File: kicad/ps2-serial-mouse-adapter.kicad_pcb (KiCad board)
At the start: 2 copper layers, 68.9 x 34 mm, 8 parts, among them U1 Arduino_Nano, U2 MAX3232_HW027

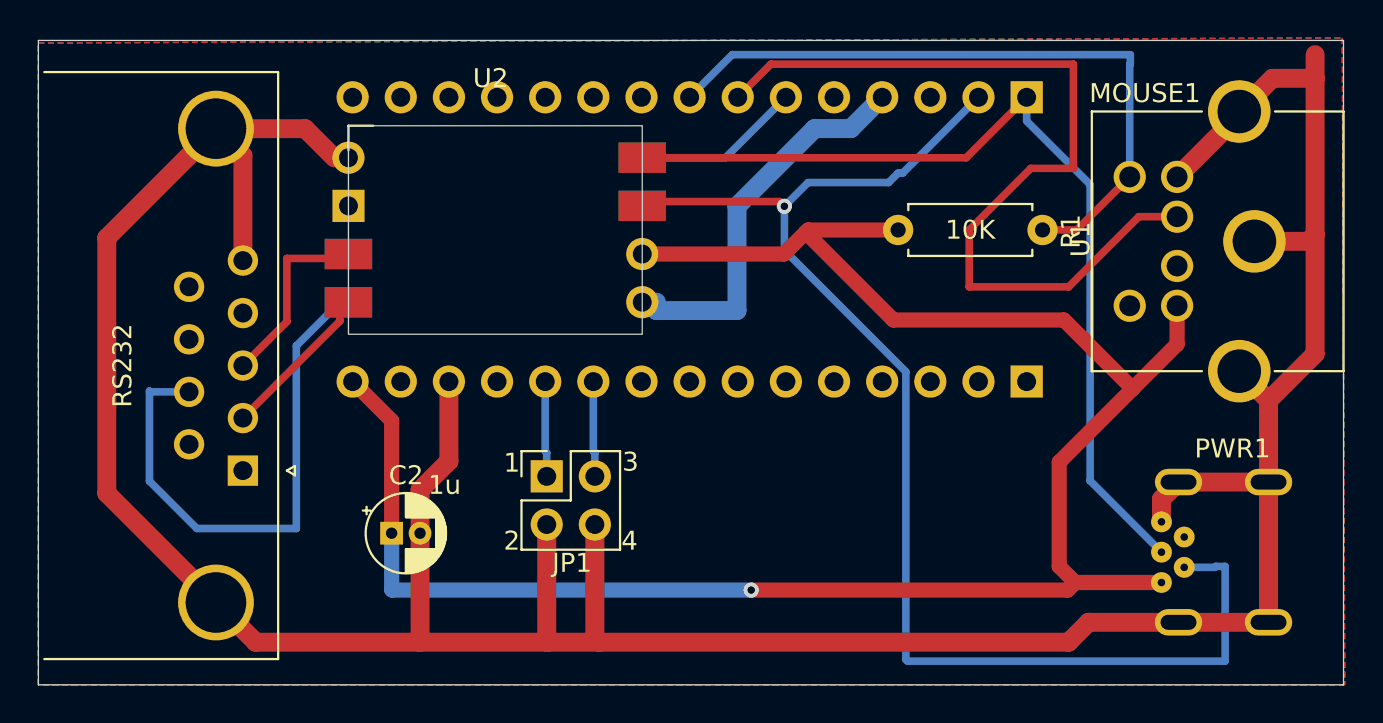
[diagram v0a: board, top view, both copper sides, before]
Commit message: flip arduino and fix pinout. Change usb-mini plug to a pinheader row. Add pads for U2
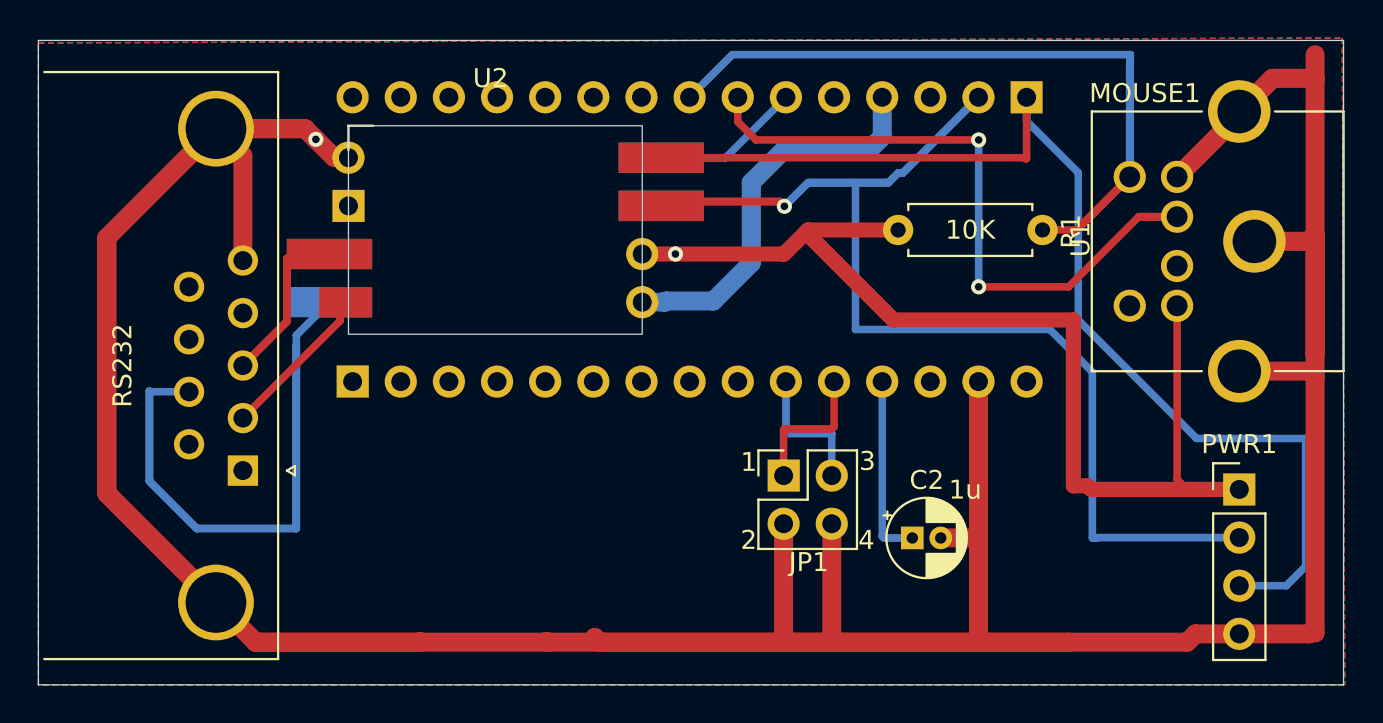
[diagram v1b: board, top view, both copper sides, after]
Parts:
- PWR1: footprint ps2-serial-mouse-adapter:USB_Mini-B-Jing_Extension_LSCS_C46398 -> PinHeader_1x04_P2.54mm_Vertical
- moved C2 27.5 mm to (127.4, 81.0)
- moved JP1 12.5 mm to (120.6, 77.7)
- moved PWR1 5.27 mm to (144.6, 78.4), turned to 0 degrees
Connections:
- PWR1 pad 4: unconnected-(PWR1-ID-Pad4) -> GND
- U1 pad 27: unconnected-(U1-VIN-Pad27) -> VBUS
- U1 pad 28: GND -> unconnected-(U1-RST-Pad28)
- U1 pad 29: unconnected-(U1-RST-Pad29) -> GND
- U1 pad 30: VBUS -> unconnected-(U1-VIN-Pad30)
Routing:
- net GND: track 204.0 -> 271.6 mm, vias 0 -> 1
- net VBUS: track 104.4 -> 77.0 mm
- net Net-(U2-RS232_RXD2): track 28.5 -> 51.5 mm
- net TX: track 48.1 -> 61.9 mm
- net CLK: track 36.4 -> 46.8 mm
- net DATA: track 46.3 -> 36.2 mm, vias 0 -> 2
- net Net-(U2-RS232_RXD1): track 10.1 -> 19.8 mm
- net RX: track 70.6 -> 77.8 mm
- net Net-(JP1-Pin_1): track 5.03 -> 7.53 mm
- net Net-(JP1-Pin_3): track 5.03 -> 7.49 mm
- net Net-(U2-RS232_TXD1): track 8.24 -> 9.23 mm

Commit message: Fix positioning of no_connect and global_label in PS2 Serial Mouse Adapter schematic
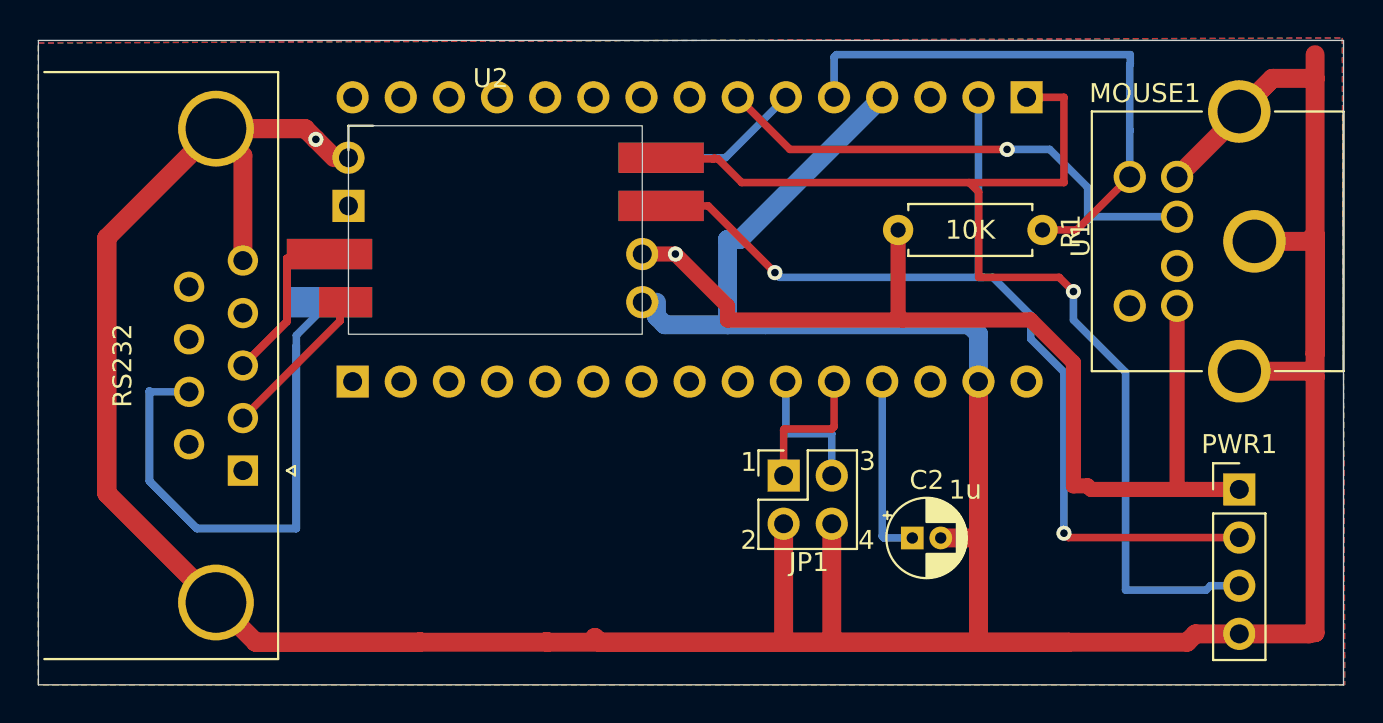
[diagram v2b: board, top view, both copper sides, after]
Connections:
- U1 pad 5: unconnected-(U1-D2-Pad5) -> CLK
- U1 pad 8: CLK -> unconnected-(U1-D5-Pad8)
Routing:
- net RX: track 77.8 -> 53.7 mm, vias 1 -> 2
- net CLK: track 46.8 -> 30.1 mm
- net GND: track 271.6 -> 287.9 mm
- net VBUS: track 77.0 -> 64.9 mm
- net DATA: track 36.2 -> 27.0 mm, vias 2 -> 1
- net RTS: track 8.45 -> 7.90 mm
- net TX: track 61.9 -> 61.8 mm, vias 0 -> 1

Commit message: Refactor code structure for improved readability and maintainability. Removed unused Rx from design, unused for this purpose. Added activity LEDs for pre and post MAX232 on TX. Aditional bipolar filter cap on Vcc and pull up resistor on Data line. Added debug mode  jumper.
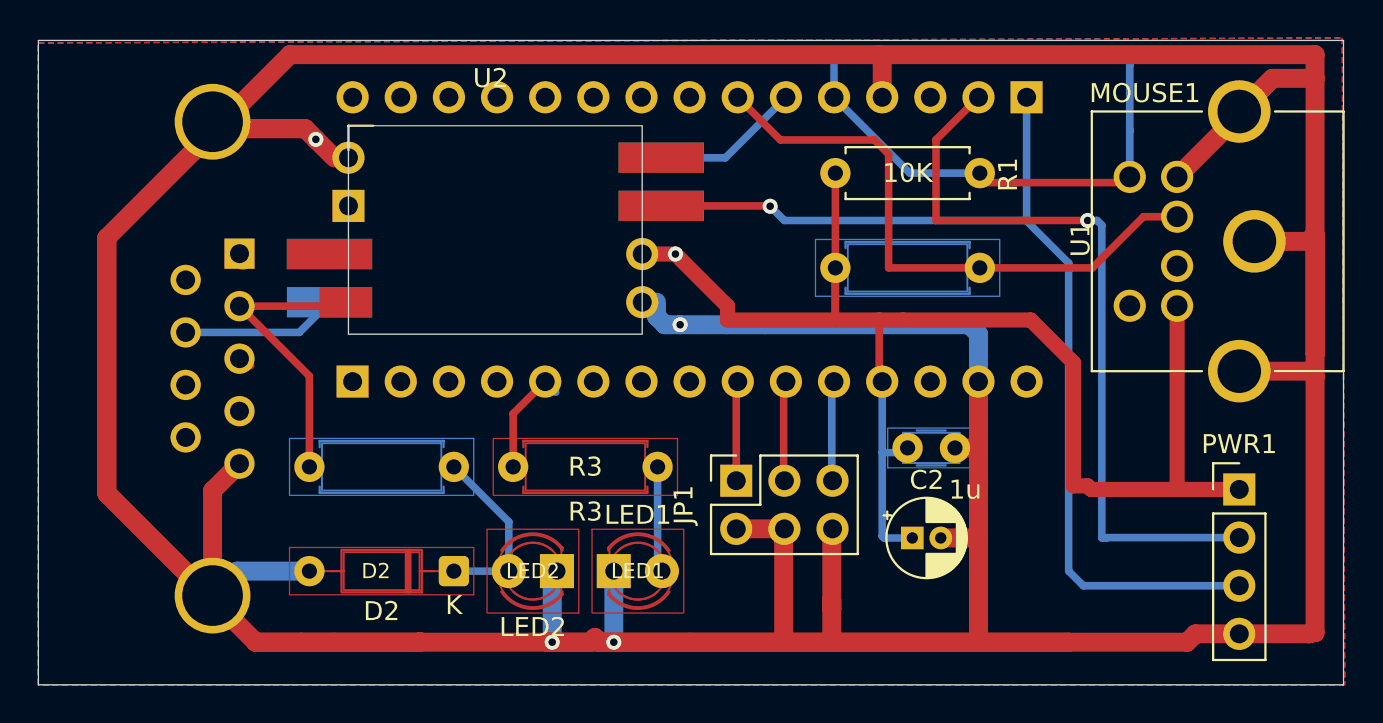
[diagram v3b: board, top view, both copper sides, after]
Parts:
- added C3: 100nF, Capacitor_THT:C_Disc_D3.0mm_W1.6mm_P2.50mm, B.Cu at (127.1, 76.2)
- added D2: 1N4148, Diode_THT:D_DO-35_SOD27_P7.62mm_Horizontal, F.Cu at (103.2, 82.7)
- added LED1: LED, LED_THT:LED_D3.0mm, F.Cu at (111.6, 82.7)
- added LED2: LED, LED_THT:LED_D3.0mm, F.Cu at (108.6, 82.7)
- added R2: 10K, Resistor_THT:R_Axial_DIN0207_L6.3mm_D2.5mm_P7.62mm_Horizontal, B.Cu at (123.3, 66.7)
- added R3: 330, Resistor_THT:R_Axial_DIN0207_L6.3mm_D2.5mm_P7.62mm_Horizontal, F.Cu at (114.0, 77.2)
- added R4: 2.2k, Resistor_THT:R_Axial_DIN0207_L6.3mm_D2.5mm_P7.62mm_Horizontal, B.Cu at (103.2, 77.2)
- JP1: value Conn_02x02_Odd_Even -> Conn_02x03_Odd_Even; footprint Connector_PinSocket_2.54mm:PinSocket_2x02_P2.54mm_Vertical -> Connector_PinSocket_2.54mm:PinSocket_2x03_P2.54mm_Vertical
- PWR1: value USB_B_Mini -> Conn_Panel_1x04; footprint PinHeader_1x04_P2.54mm_Vertical -> Connector_PinHeader_2.54mm:PinHeader_1x04_P2.54mm_Vertical
- RS232: moved to B.Cu
- moved RS232 11.4 mm to (91.9, 66.0), turned to 90 degrees
- moved R1 4.47 mm to (123.3, 61.7)
- moved JP1 2.51 mm to (118.1, 78.0)
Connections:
- net Net-(JP1-Pin_1) renamed JP12
- net Net-(JP1-Pin_3) renamed JP34
- RS232 pad 3: Net-(U2-RS232_RXD1) -> unconnected-(RS232-Pad3)
- U1 pad 20: unconnected-(U1-A1-Pad20) -> Net-(U1-A1)
- U1 pad 24: unconnected-(U1-A5-Pad24) -> JP56
- U2 pad 10: RX -> TX
- U2 pad 5: Net-(U2-RS232_RXD1) -> unconnected-(U2-RS232_RXD1-Pad5)
- U2 pad 9: TX -> unconnected-(U2-TTL_TXD1-Pad9)
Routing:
- net GND: track 287.9 -> 353.6 mm, vias 1 -> 4
- net Net-(U2-RS232_RXD2): track 51.5 -> 8.25 mm
- net Net-(U2-RS232_RXD1): track 19.8 -> 0.00 mm
- net RX: track 53.7 -> 40.0 mm, vias 2 -> 1
- net CLK: track 30.1 -> 41.7 mm
- net VBUS: track 64.9 -> 75.5 mm
- net Net-(D2-K): track 0.00 -> 9.60 mm
- net TX: track 61.8 -> 55.3 mm
- net Net-(U2-RS232_TXD1): track 9.23 -> 15.4 mm
- net Net-(U1-A1): track 0.00 -> 5.99 mm
- net Net-(LED1-A): track 0.00 -> 5.60 mm
- net JP56: track 0.00 -> 5.26 mm
- net DATA: track 27.0 -> 31.5 mm, vias 1 -> 0
- net JP12: track 7.53 -> 5.01 mm
- net JP34: track 7.49 -> 5.01 mm
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
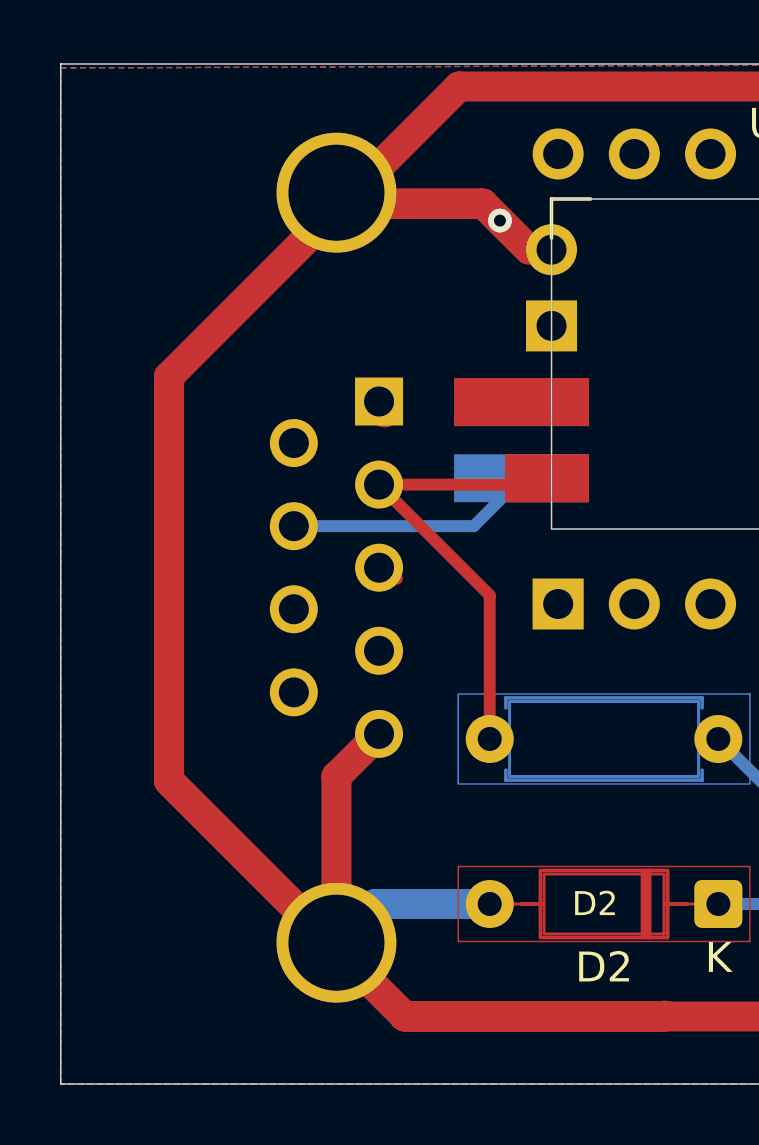
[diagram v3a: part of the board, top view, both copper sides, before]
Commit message: Flip RS232
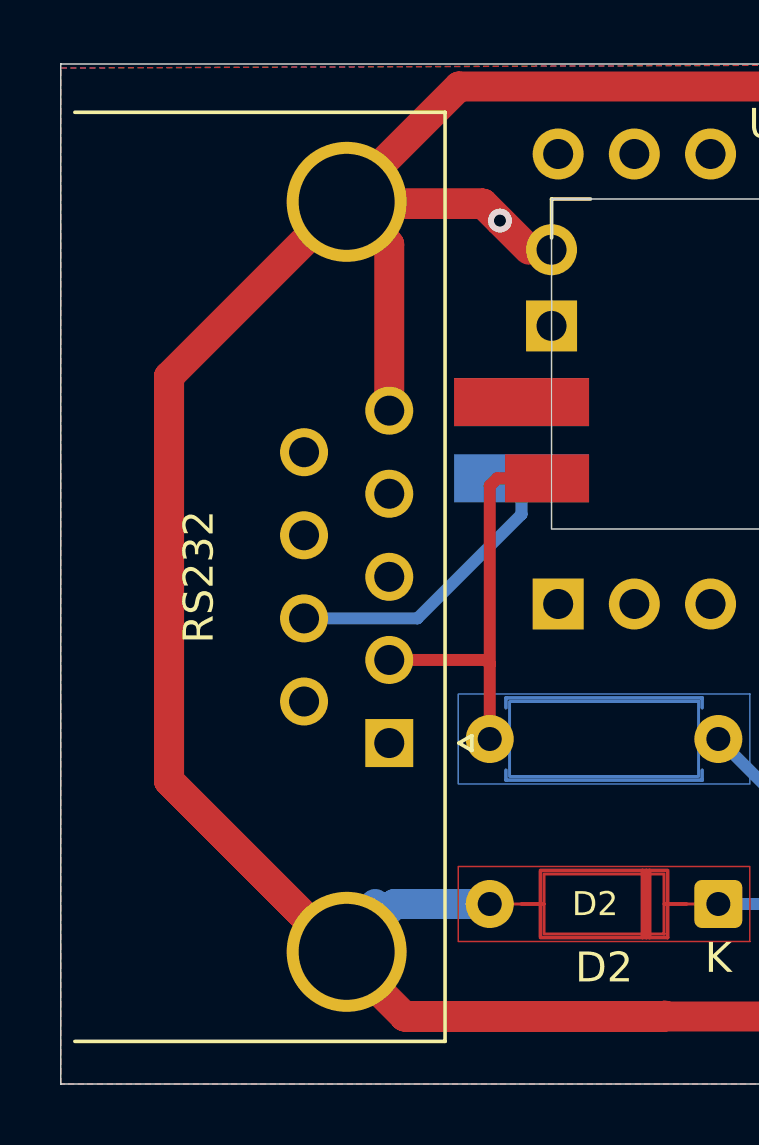
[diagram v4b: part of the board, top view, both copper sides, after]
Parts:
- RS232: moved to F.Cu
- moved RS232 11.4 mm to (92.2, 77.4), turned to -90 degrees
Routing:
- net Net-(U2-RS232_RXD2): track 8.25 -> 10.1 mm
- net GND: track 353.6 -> 355.2 mm
- net Net-(U2-RS232_TXD1): track 15.4 -> 13.9 mm
